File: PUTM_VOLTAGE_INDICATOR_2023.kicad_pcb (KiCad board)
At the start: 2 copper layers, 39 parts, among them IC1 LM211DT, J1 HV+, J2 HV-, Q1 TK3P80E,RQ, U1 LT8316EFE

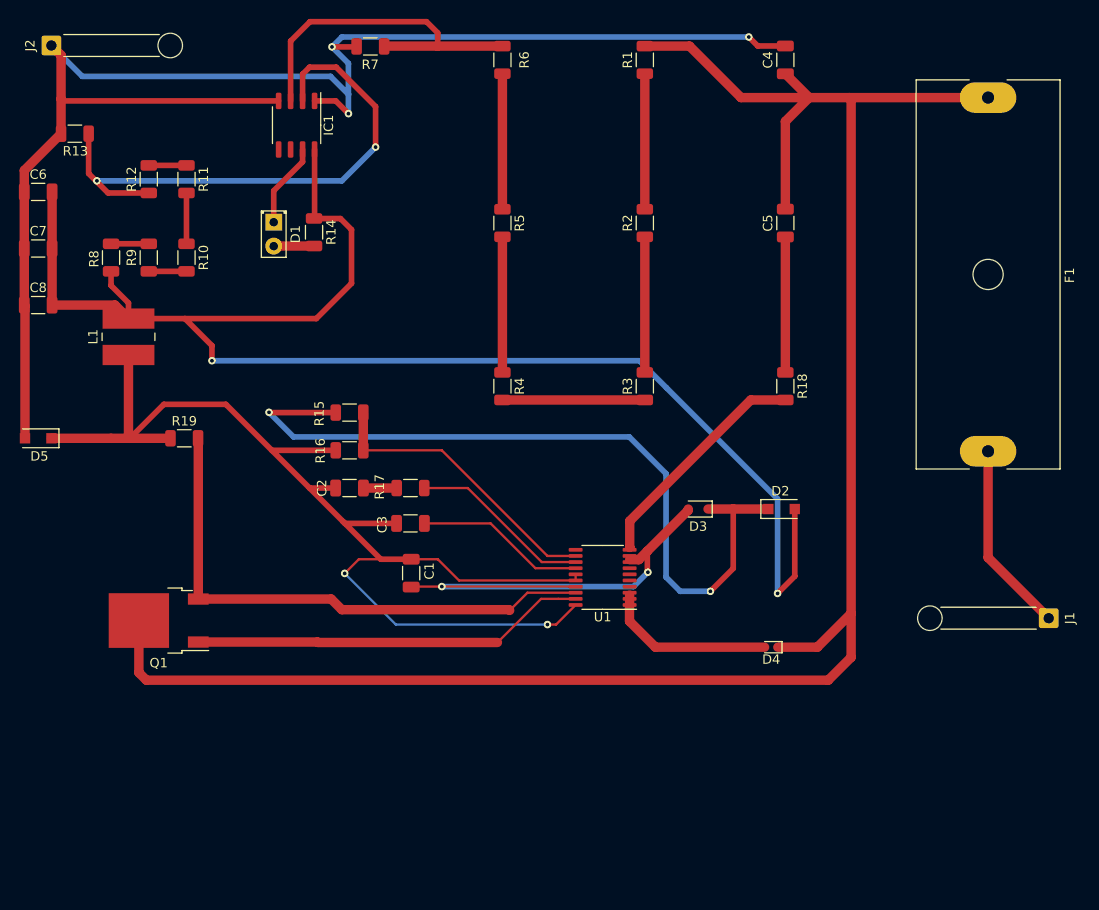
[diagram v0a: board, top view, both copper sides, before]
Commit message: resistors change; elements placed; new footprints
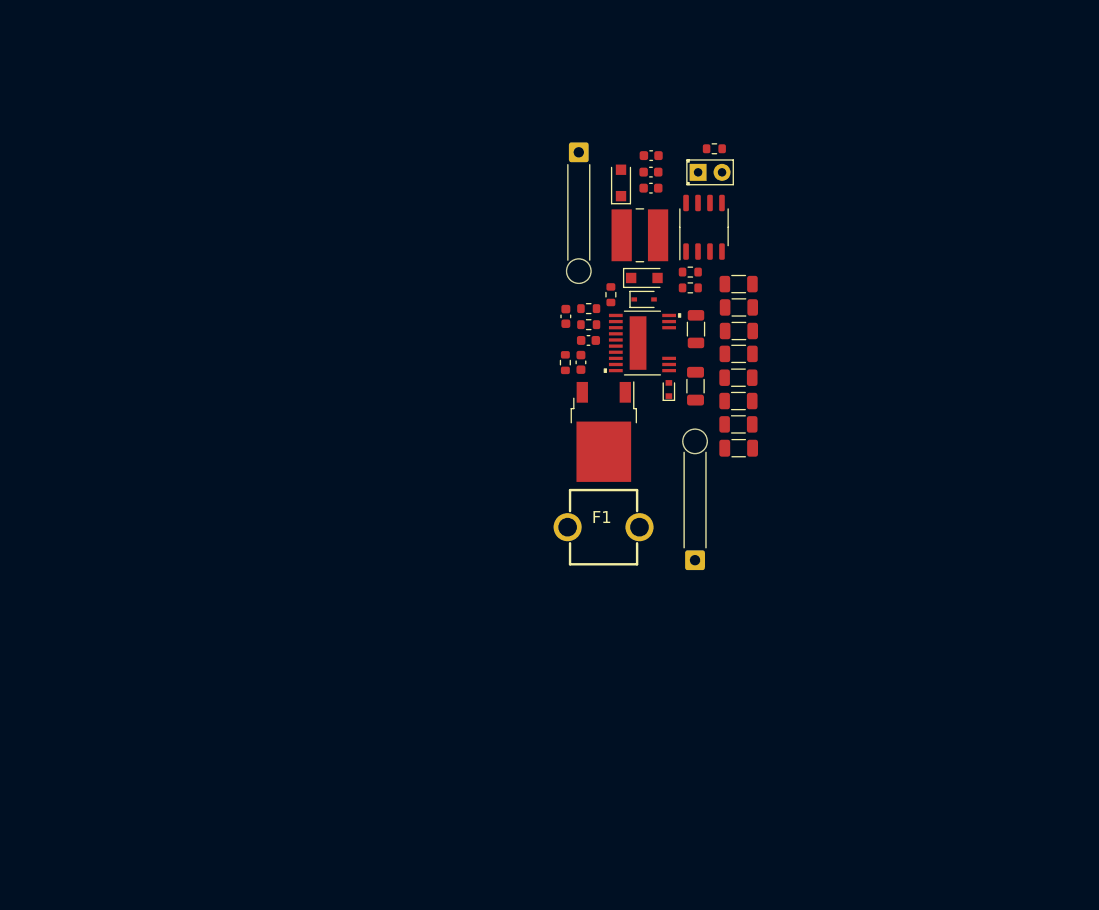
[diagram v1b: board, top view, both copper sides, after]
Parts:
- removed R10, R11, R9: 10kR, Resistor_SMD:R_1206_3216Metric
- removed R12: 3kR, Resistor_SMD:R_1206_3216Metric
- C1, C2, C3, C6, C7, C8: footprint Capacitor_SMD:C_1206_3216Metric -> Capacitor_SMD:C_0603_1608Metric
- F1: footprint Fuse:Fuseholder_Cylinder-6.3x32mm_Schurter_0031-8002_Horizontal_Open -> vindicator:01020071Z-FUSE-CLIP
- R13: value 10kR -> 196R; footprint Resistor_SMD:R_1206_3216Metric -> Resistor_SMD:R_0603_1608Metric
- R14, R15, R16, R17, R19: footprint Resistor_SMD:R_1206_3216Metric -> Resistor_SMD:R_0603_1608Metric
- R6: value 90kR -> 100kR
- R8: value 100kR -> 2.2kR; footprint Resistor_SMD:R_1206_3216Metric -> Resistor_SMD:R_0603_1608Metric
- U1: footprint Package_SO:TSSOP-20_4.4x6.5mm_P0.65mm -> vindicator:LT8316EFE
- moved D5 67.5 mm to (144.2, 71.6), turned to 90 degrees
- moved R13 66.9 mm to (151.5, 81.1)
- moved C8 66.1 mm to (147.3, 72.2)
- moved C7 65.5 mm to (147.3, 70.5)
- moved C6 65.1 mm to (147.3, 68.7)
- moved R8 61.5 mm to (151.5, 82.8), turned to 180 degrees
- moved F1 61.1 mm to (142.3, 108.1), turned to 0 degrees
- moved J2 57.1 mm to (139.7, 68.4), turned to 0 degrees
- moved L1 55.3 mm to (146.2, 77.2), turned to 0 degrees
- moved Q1 51.3 mm to (142.3, 98.0), turned to -90 degrees
- moved R7 46.5 mm to (156.6, 82.3), turned to 180 degrees
- moved D1 45.3 mm to (152.3, 70.5), turned to 0 degrees
- moved IC1 44.5 mm to (152.9, 76.3), turned to 90 degrees
- moved R14 43.4 mm to (154.1, 68.0), turned to 0 degrees
- moved C4 41.5 mm to (156.6, 99.8), turned to 0 degrees
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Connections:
- IC1 pad 2: Net-(IC1-Pad2) -> Net-(R8-Pad1)
- R13 pad 2: Net-(IC1-Pad2) -> Net-(R8-Pad1)
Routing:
- net +VDC: track 206.2 -> 0.00 mm
- net GND: track 164.0 -> 0.00 mm, vias 3 -> 0
- net +12V: track 160.6 -> 0.00 mm, vias 2 -> 0
- net Net-(C1-Pad2): track 126.0 -> 0.00 mm, vias 2 -> 0
- net Net-(D2-Pad1): track 84.3 -> 0.00 mm, vias 2 -> 0
- net Net-(IC1-Pad2): track 59.4 -> 0.00 mm, vias 2 -> 0
- net Net-(Q1-Pad3): track 58.4 -> 0.00 mm
- net Net-(C1-Pad1): track 50.7 -> 0.00 mm, vias 2 -> 0
- net Net-(Q1-Pad1): track 41.9 -> 0.00 mm
- net Net-(IC1-Pad3): track 37.2 -> 0.00 mm
- net Net-(R15-Pad1): track 31.2 -> 0.00 mm
- net Net-(R18-Pad2): track 24.6 -> 0.00 mm
- net Net-(F1-Pad2): track 20.4 -> 0.00 mm
- net Net-(R17-Pad2): track 19.3 -> 0.00 mm
- net Net-(D4-Pad2): track 18.2 -> 0.00 mm
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
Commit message: pcb edit
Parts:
- C2, C3: footprint Capacitor_SMD:C_0603_1608Metric -> Capacitor_SMD:C_1812_4532Metric
- C4: footprint Capacitor_SMD:C_1206_3216Metric -> Capacitor_SMD:C_1812_4532Metric
- C6, C7, C8: footprint Capacitor_SMD:C_0603_1608Metric -> Capacitor_SMD:C_1206_3216Metric
- moved R14 71.0 mm to (113.1, 126.0), turned to 90 degrees
- moved D1 68.0 mm to (115.6, 127.7), turned to 90 degrees
- moved R1 63.2 mm to (104.3, 132.7), turned to 90 degrees
- moved R2 61.2 mm to (108.6, 132.8), turned to -90 degrees
- moved R3 59.5 mm to (113.0, 132.8), turned to 90 degrees
- moved R4 58.3 mm to (117.3, 132.8), turned to -90 degrees
- moved R5 57.5 mm to (121.3, 132.8), turned to 90 degrees
- moved R7 57.4 mm to (129.3, 132.8), turned to 90 degrees
- moved R6 57.3 mm to (125.3, 132.8), turned to -90 degrees
- moved IC1 57.0 mm to (127.8, 127.5), turned to 180 degrees
- moved D2 55.7 mm to (109.0, 122.8), turned to 180 degrees
- moved R18 54.2 mm to (106.7, 116.6), turned to -90 degrees
- moved J1 53.8 mm to (104.9, 137.6), turned to 90 degrees
- moved C5 52.1 mm to (104.2, 113.7), turned to 90 degrees
- moved D3 51.9 mm to (109.6, 120.4), turned to 180 degrees
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
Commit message: Update PUTM_VOLTAGE_INDICATOR_2023.kicad_pcb
pcb update
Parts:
- moved R7 34.9 mm to (131.8, 98.0)
- moved R3 34.9 mm to (114.0, 98.0)
- moved R4 34.9 mm to (118.3, 98.0)
- moved R5 34.9 mm to (122.3, 97.9)
- moved R6 34.9 mm to (126.3, 98.0)
- moved R1 34.9 mm to (105.3, 97.9)
- moved R2 34.9 mm to (109.6, 97.9)
- moved D1 22.2 mm to (127.3, 108.8), turned to 180 degrees
- moved R14 18.4 mm to (124.3, 111.3), turned to 0 degrees
- moved IC1 11.4 mm to (126.4, 116.2), turned to 90 degrees
- moved R19 8.92 mm to (110.1, 113.1)
- moved C8 8.35 mm to (119.8, 109.9)
- moved C7 8.26 mm to (119.8, 112.4)
- moved C6 8.25 mm to (119.7, 115.0)
- moved L1 8.15 mm to (114.0, 111.3), turned to -90 degrees
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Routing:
- net GND: track 0.00 -> 87.5 mm, vias 0 -> 2
- net Net-(C1-Pad2): track 0.00 -> 62.1 mm, vias 0 -> 2
- net +12V: track 0.00 -> 60.8 mm, vias 0 -> 4
- net +VDC: track 0.00 -> 51.6 mm
- net Net-(IC1-Pad3): track 0.00 -> 37.5 mm, vias 0 -> 2
- net Net-(C1-Pad1): track 0.00 -> 29.7 mm, vias 0 -> 2
- net Net-(Q1-Pad1): track 0.00 -> 17.2 mm
- net Net-(Q1-Pad3): track 0.00 -> 14.0 mm
- net Net-(F1-Pad2): track 0.00 -> 13.6 mm
- net Net-(IC1-Pad2): track 0.00 -> 9.62 mm
- net Net-(R15-Pad1): track 0.00 -> 8.80 mm
- net Net-(R17-Pad2): track 0.00 -> 6.84 mm
- net Net-(D1-Pad1): track 0.00 -> 5.43 mm
- net Net-(C3-Pad1): track 0.00 -> 5.30 mm
- net Net-(D2-Pad1): track 0.00 -> 5.05 mm
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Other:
- board outline added: 41 x 41.7 mm

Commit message: pcb update
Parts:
- added ?: , , F.Cu at (129.3, 140.5)
- added ?: , , F.Cu at (97.8, 90.1)
- added ?: , , F.Cu at (129.2, 90.0)
- added ?: , , F.Cu at (99.0, 141.8)
- added G***: LOGO, SignatureBox25mm, F.Cu at (113.7, 140.2)
- added G***: LOGO, PUTM_LOGO_18mm, F.Cu at (114.2, 89.6)
- C2, C3: footprint Capacitor_SMD:C_1812_4532Metric -> Capacitor_SMD:C_0603_1608Metric
- moved C2 4.66 mm to (120.5, 123.7), turned to -90 degrees
- moved R16 4.47 mm to (117.9, 124.5), turned to 180 degrees
- moved R17 4.35 mm to (117.9, 122.9), turned to 180 degrees
- moved C3 4.02 mm to (117.9, 121.2)
- moved R15 2.25 mm to (112.9, 125.5), turned to 180 degrees
- moved R18 1.50 mm to (105.3, 122.8), turned to 0 degrees
- moved C1 0.51 mm to (119.7, 119.0), turned to 0 degrees
- moved J1 0.21 mm to (103.7, 132.6)
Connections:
- U1 pad EPAD: GND -> Net-(C1-Pad2)
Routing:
- net GND: track 87.5 -> 54.7 mm, vias 2 -> 5
- net Net-(C1-Pad2): track 62.1 -> 52.4 mm
- net Net-(C1-Pad1): track 29.7 -> 34.2 mm
- net Net-(R17-Pad2): track 6.84 -> 2.60 mm
- net Net-(C3-Pad1): track 5.30 -> 2.42 mm
- net Net-(R15-Pad1): track 8.80 -> 6.95 mm
- net +12V: track 60.8 -> 62.1 mm
- net Net-(D2-Pad1): track 5.05 -> 3.99 mm
- net Net-(R18-Pad2): track 3.24 -> 2.65 mm
- added copper zone on B.Cu, net GND
- added copper zone on F.Cu, net GND
- added copper zone on F.Cu, net Net-(C1-Pad2)
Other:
- board size 41 x 41.7 mm -> 42.4 x 61.1 mm

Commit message: pcb update
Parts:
- moved D2 4.14 mm to (112.8, 126.6), turned to 90 degrees
- moved R15 3.75 mm to (115.5, 128.2)
- moved D3 1.16 mm to (110.7, 126.0), turned to 90 degrees
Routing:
- net +12V: track 62.1 -> 47.6 mm
- net Net-(C1-Pad1): track 34.2 -> 22.4 mm
- net Net-(C1-Pad2): track 52.4 -> 57.4 mm
- net Net-(D2-Pad1): track 3.99 -> 4.66 mm
- added copper zone on F.Cu, net +12V

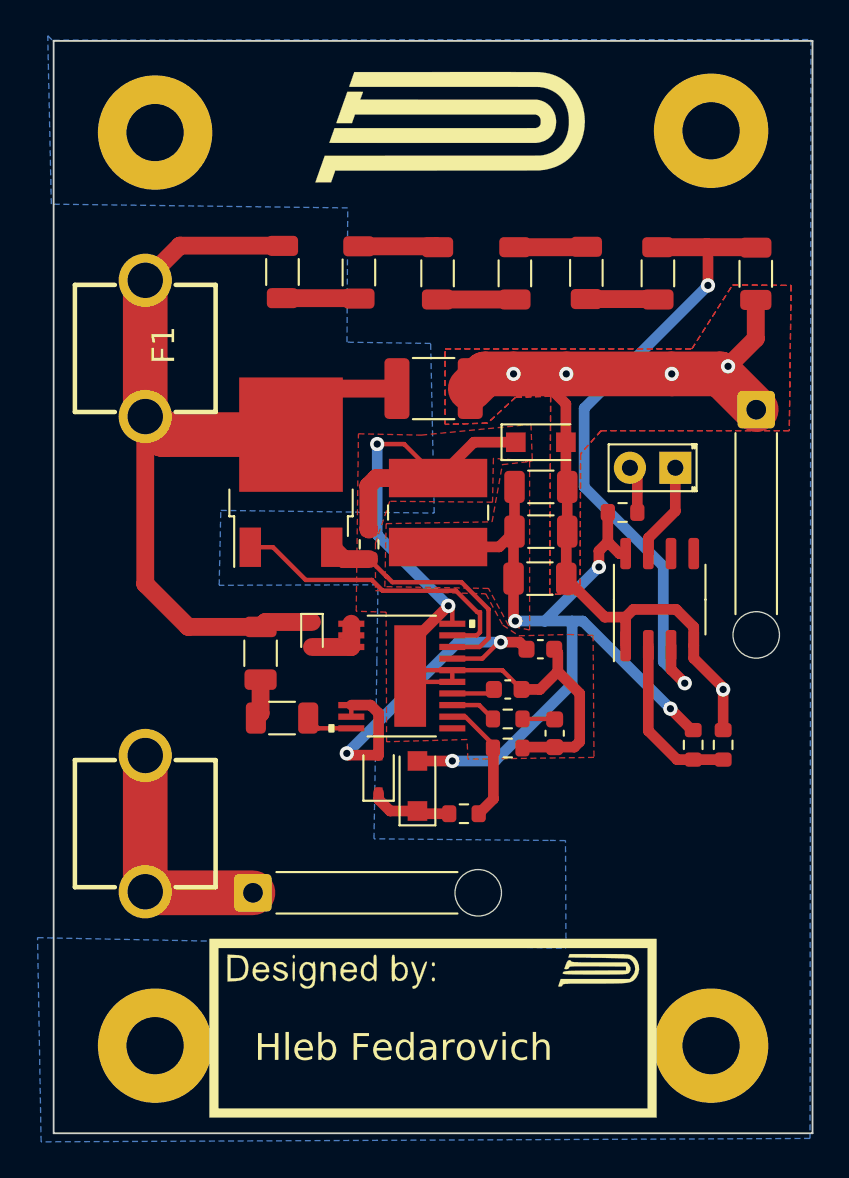
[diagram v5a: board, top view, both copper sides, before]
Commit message: cleanup
cleaned up some traces, fixed DRC errors
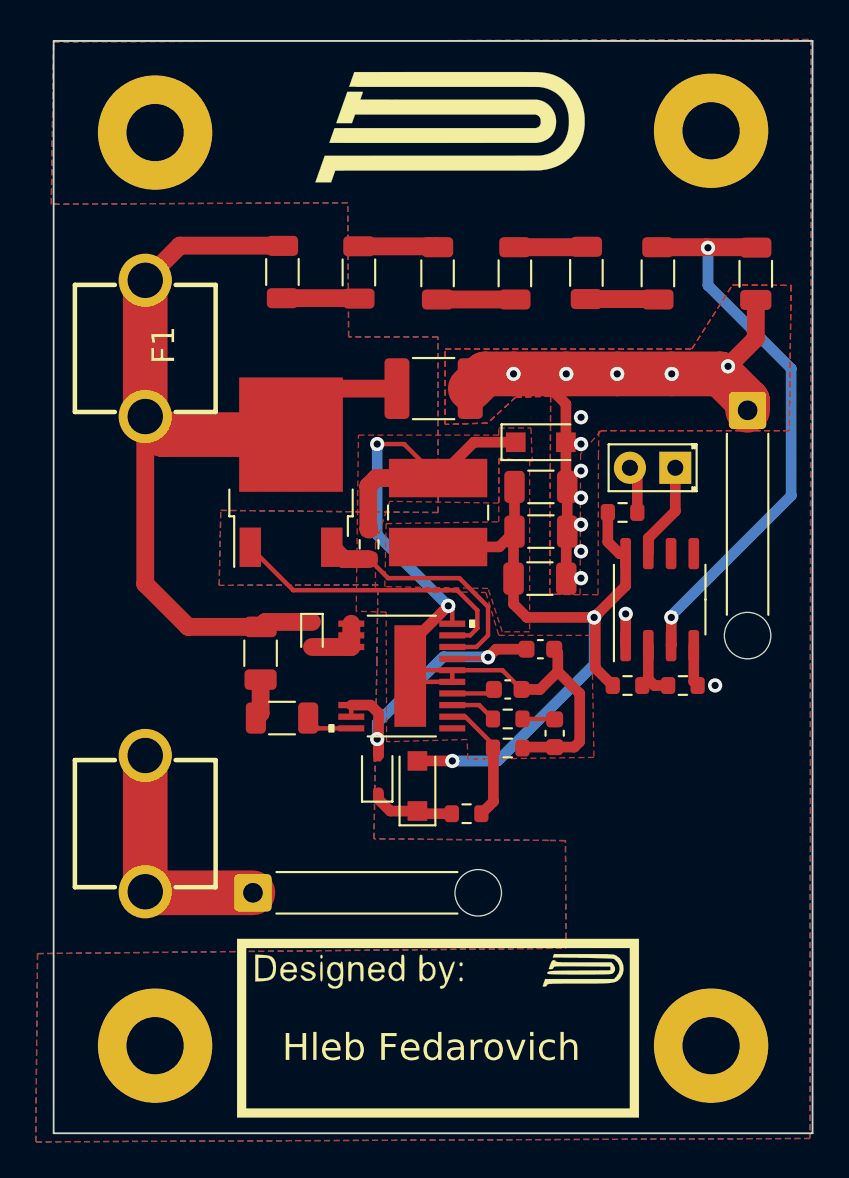
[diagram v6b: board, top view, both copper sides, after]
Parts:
- moved R8 4.95 mm to (124.6, 121.0), turned to 180 degrees
- moved R13 4.01 mm to (127.7, 121.0), turned to 180 degrees
- moved G*** 1.55 mm to (115.2, 140.2)
- moved J2 0.48 mm to (131.3, 105.6)
- moved R15 0.15 mm to (115.6, 128.2)
- moved D3 0.09 mm to (110.6, 126.0)
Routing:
- net GND: track 54.7 -> 42.0 mm, vias 5 -> 14
- net Net-(IC1-Pad2): track 9.62 -> 3.62 mm
- net +12V: track 47.6 -> 42.5 mm, vias 4 -> 2
- net Net-(IC1-Pad3): track 37.5 -> 32.5 mm
- net Net-(C1-Pad1): track 22.4 -> 18.7 mm

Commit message: symbol changed / resistor values changed
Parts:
- R13: value 196R -> 400R
- R8: value 2.2kR -> 5kR
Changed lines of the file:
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@@
       (effects (font (size 1 1) (thickness 0.15)))
     )
-    (fp_text value "2.2kR" (at 0 1.43) (layer "F.Fab") hide
+    (fp_text value "5kR" (at 0 1.43) (layer "F.Fab") hide
       (effects (font (size 1 1) (thickness 0.15)))
     )
@@
       (effects (font (size 1 1) (thickness 0.15)))
     )
-    (fp_text value "196R" (at 0.275 1.425) (layer "F.Fab") hide
-      (effects (font (size 1 1) (thickness 0.15)))
-    )
+    (fp_text value "400R" (at 0.275 1.425) (layer "F.Fab") hide
+      (effects (font (size 1 1) (thickness 0.15)))
+    )
